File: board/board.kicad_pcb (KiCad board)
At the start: 2 copper layers, 21 x 61 mm, 16 parts, among them J1 002_SPI_2x5, J3 007_ADC_2x5, J4 007_ADC_2x5, J5 007_ADC_2x5, J6 007_ADC_2x5, U1 ADS131M08, Y1 8MhZ

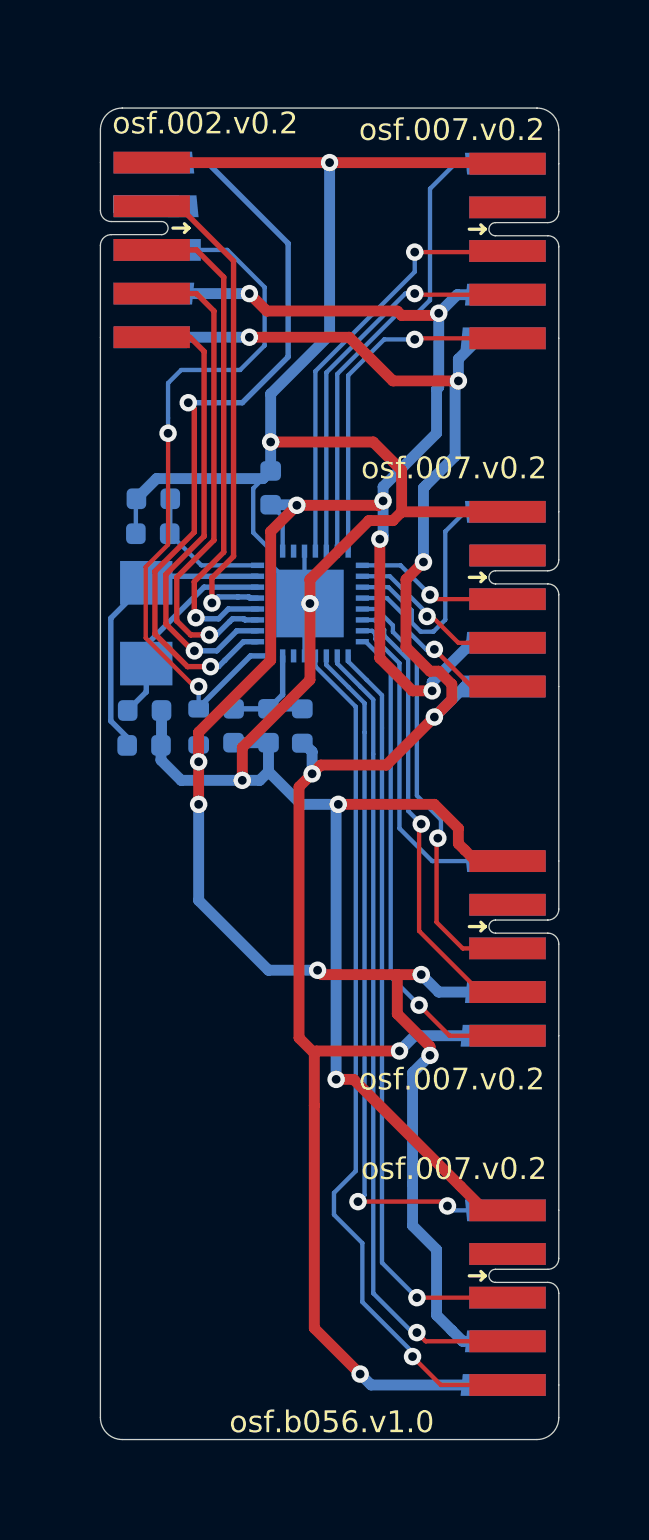
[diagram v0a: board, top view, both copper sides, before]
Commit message: fixed footprint and added pours
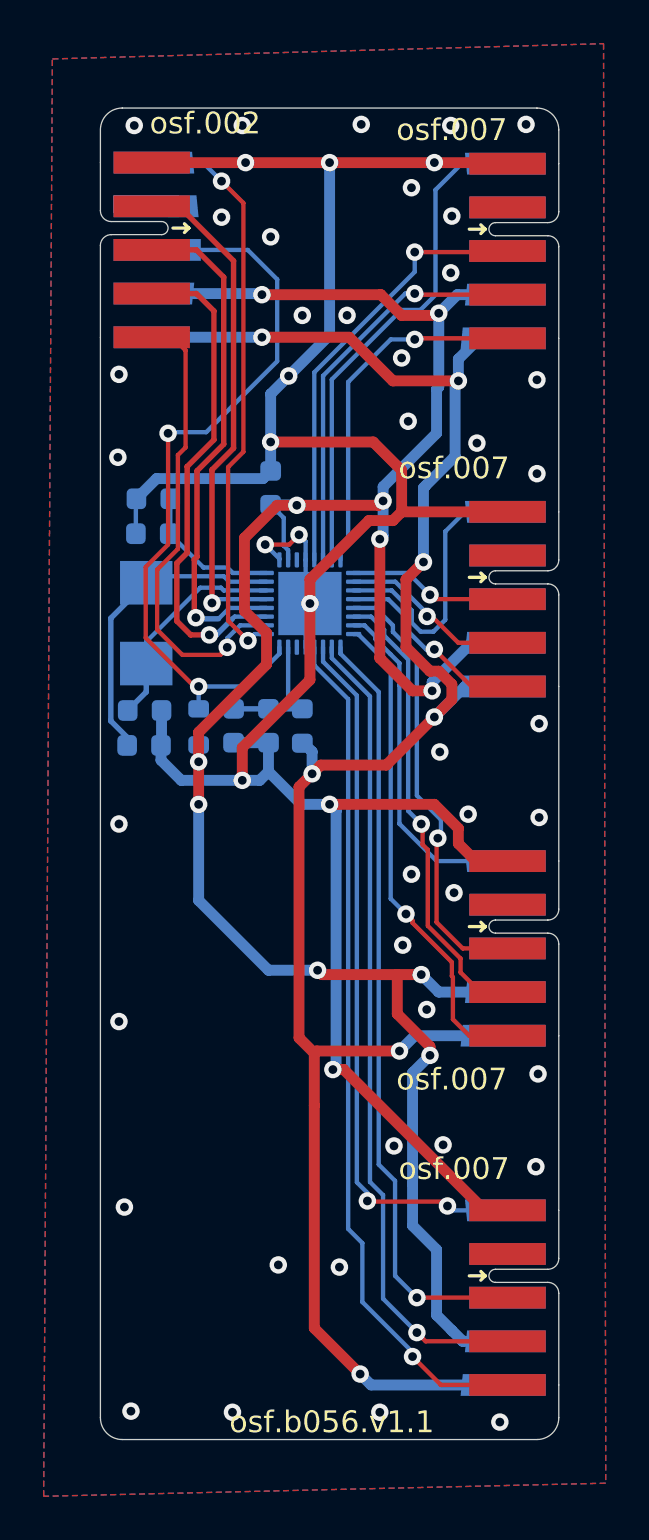
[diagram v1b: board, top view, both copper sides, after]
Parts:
- U1: footprint Package_DFN_QFN:WQFN-32-1EP_5x5mm_P0.5mm_EP3.1x3.1mm -> Package_DFN_QFN:QFN-32-1EP_4x4mm_P0.4mm_EP2.9x2.9mm
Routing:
- net /adc/~{CS}: track 35.6 -> 26.6 mm
- net GND: track 128.3 -> 124.0 mm, vias 6 -> 51
- net +3.3V: track 106.4 -> 108.3 mm
- net /adc/~{RESET}: track 34.7 -> 35.5 mm
- net /adc/AIN_6P: track 33.6 -> 34.1 mm
- net Net-(C6-Pad1): track 6.24 -> 6.78 mm
- net Net-(C1-Pad2): track 9.55 -> 10.1 mm
- net /adc/AIN_4N: track 20.9 -> 21.4 mm
- net Net-(C3-Pad1): track 13.7 -> 14.2 mm
- added copper zone on B.Cu, net GND
- added copper zone on F.Cu, net GND
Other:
- board text added: "osf.002"
- board text added: "osf.007"
- board text added: "osf.b056.v1.1"
- board text removed: "osf.002.v0.2"
- board text removed: "osf.007.v0.2"
- board text removed: "osf.b056.v1.0"
